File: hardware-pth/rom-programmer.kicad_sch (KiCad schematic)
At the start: 19 parts, among them U1 74HC595, U2 74HC595, U3 28C256

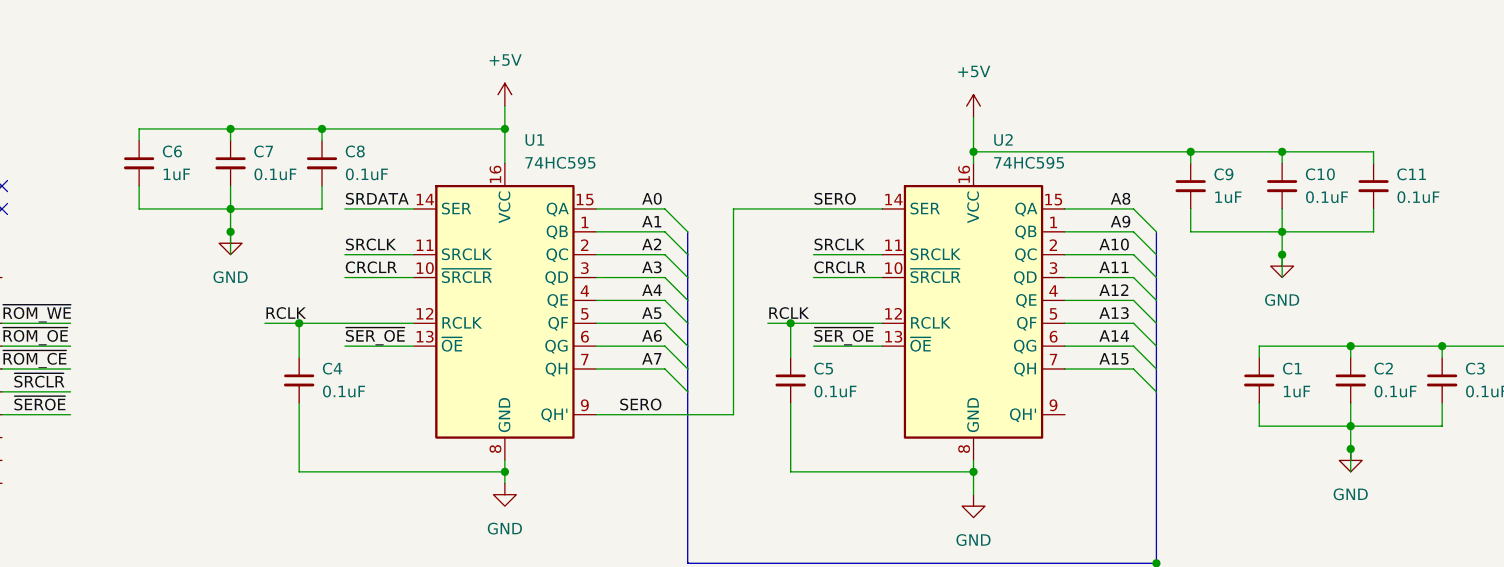
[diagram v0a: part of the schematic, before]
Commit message: Can now read a single byte from the CLI
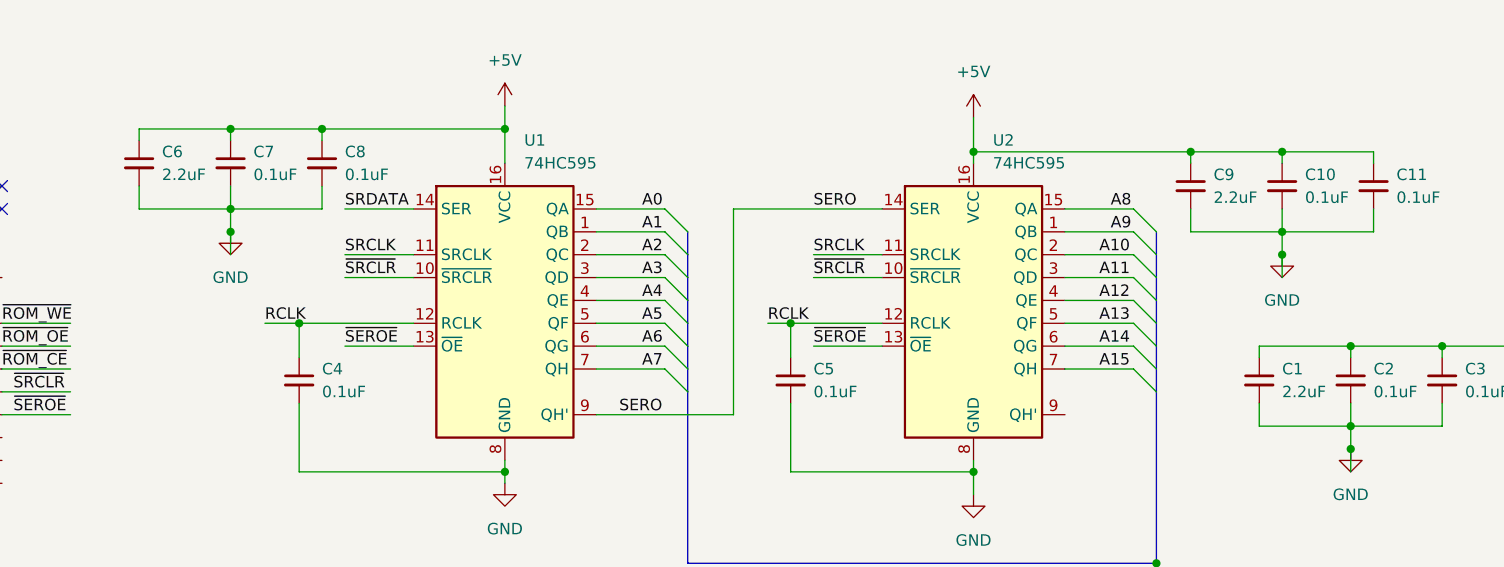
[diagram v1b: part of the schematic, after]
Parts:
- C1, C6, C9: value 1uF -> 2.2uF
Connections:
- net CRCLR is gone; now on net ~{SRCLR}: U1.10 (~{SRCLR}), U2.10 (~{SRCLR})
- net ~{SER_OE} is gone; now on net ~{SEROE}: U1.13 (~{OE}), U2.13 (~{OE})
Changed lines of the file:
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@@
 		)
 	)
-	(label "CRCLR"
+	(label "~{SRCLR}"
 		(at 99.06 46.99 0)
 		(effects
@@
 		)
 	)
-	(label "CRCLR"
+	(label "~{SRCLR}"
 		(at 151.13 46.99 0)
 		(effects
@@
 		)
 	)
-	(label "~{SER_OE}"
+	(label "~{SEROE}"
 		(at 99.06 54.61 0)
 		(effects
@@
 		)
 	)
-	(label "~{SER_OE}"
+	(label "~{SEROE}"
 		(at 151.13 54.61 0)
 		(effects
@@
 			)
 		)
-		(property "Value" "1uF"
+		(property "Value" "2.2uF"
 			(at 195.58 38.1062 0)
 			(show_name no)
@@
 			)
 		)
-		(property "Value" "1uF"
+		(property "Value" "2.2uF"
 			(at 203.2 59.6962 0)
 			(show_name no)
@@
 			)
 		)
-		(property "Value" "1uF"
+		(property "Value" "2.2uF"
 			(at 78.74 35.5662 0)
 			(show_name no)
